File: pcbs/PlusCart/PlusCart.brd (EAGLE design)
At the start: 85 x 58.7 mm, 5 parts, among them CON3 A2600

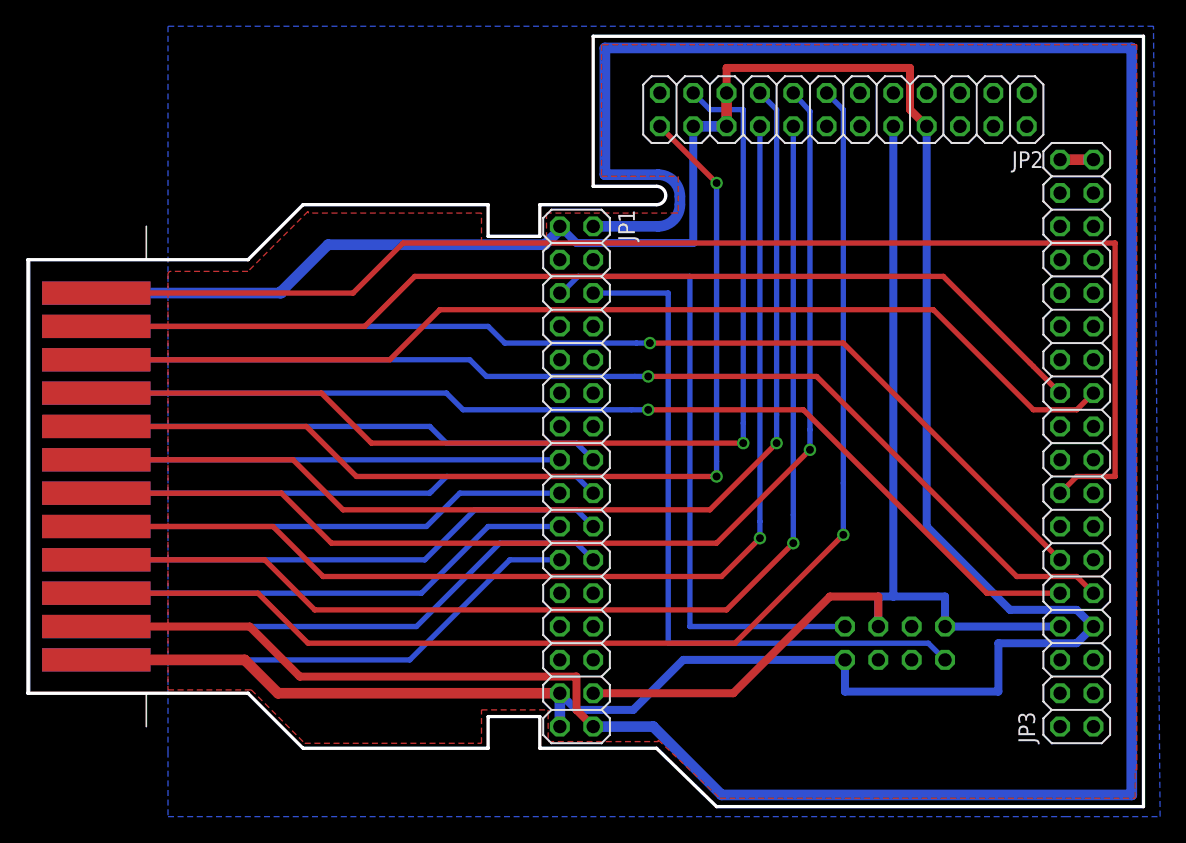
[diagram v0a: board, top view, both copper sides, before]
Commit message: Breakoutboard optimization, new gerberfiles
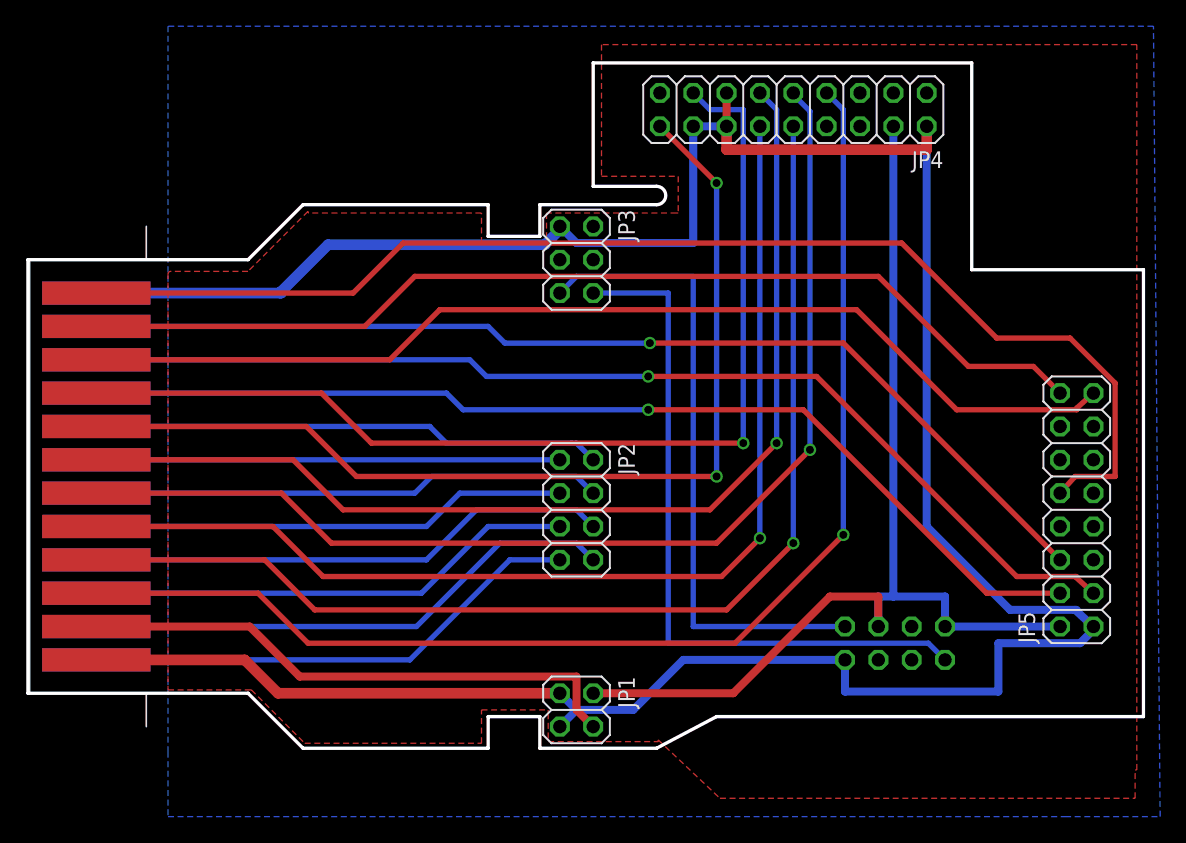
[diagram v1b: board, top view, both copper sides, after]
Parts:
- added JP5: (no value), pinhead:2X08
- added JP6: (no value), pinhead:2X04
- JP1: device pinhead:2X16 -> pinhead:2X02
- JP2: device pinhead:2X12 -> pinhead:2X04
- JP3: device pinhead:2X18 -> pinhead:2X03
- JP4: device pinhead:2X04 -> pinhead:2X09
- moved JP4 41.4 mm to (58.9, 48.0), flipped to the top, turned to 180 degrees
- moved JP3 40.6 mm to (42.4, 36.6), turned to 270 degrees
- moved JP2 36.6 mm to (42.4, 17.5), turned to 270 degrees
- moved JP1 17.8 mm to (42.4, 2.29)
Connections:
- removed net N$1: JP3.35, JP3.36
- net +3V3: now also JP1.2, JP4.4, JP5.2, JP6.2, JP6.6; no longer JP1.30, JP2.10, JP3.8, JP4.2, JP4.6
- net A0: now also JP2.2; no longer JP1.16
- net A1: now also JP2.1; no longer JP1.15
- net A10: now also JP4.9; no longer JP2.15
- net A11: now also JP4.12; no longer JP2.18
- net A12: now also JP4.11; no longer JP2.17
- net A2: now also JP2.4; no longer JP1.18
- net A3: now also JP2.3; no longer JP1.17
- net A4: now also JP2.6; no longer JP1.20
- net A5: now also JP2.5; no longer JP1.19
- net A6: now also JP2.8; no longer JP1.22
- net A7: now also JP2.7; no longer JP1.21
- net A8: now also JP4.7; no longer JP2.13
- net A9: now also JP4.10; no longer JP2.16
- net D0: now also JP5.4; no longer JP3.10
- net D1: now also JP5.3; no longer JP3.9
- net D2: now also JP5.6; no longer JP3.12
- net D3: now also JP5.10; no longer JP3.16
- net D4: now also JP5.16; no longer JP3.22
- net D5: now also JP5.15; no longer JP3.21
- net D6: now also JP4.15; no longer JP2.21
- net D7: now also JP4.18; no longer JP2.24
- net GND: now also JP1.3, JP3.1, JP4.13, JP4.14, JP4.16, JP4.2, JP5.1, JP6.7; no longer JP1.29, JP1.31, JP2.19, JP2.20, JP2.22, JP2.8, JP3.7, JP4.7
- net USART1_RX: now also JP3.5, JP6.8; no longer JP1.5, JP4.8
- net USART1_TX: now also JP3.6, JP6.1; no longer JP1.6, JP4.1
- net VCC: now also JP1.4; no longer JP1.2, JP1.32
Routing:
- net VCC: track 206.7 -> 42.5 mm
- net D3: track 101.7 -> 95.5 mm
- net N$1: track 2.54 -> 0.00 mm
- net GND: track 217.9 -> 215.7 mm
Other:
- board size 85 x 58.7 mm -> 85 x 52.2 mm
- board text added: "PlusCart V1.2 by W.Stubig (c) 2019"
- board text removed: "PlusCart V1.1 by W.Stubig (c) 2019"
